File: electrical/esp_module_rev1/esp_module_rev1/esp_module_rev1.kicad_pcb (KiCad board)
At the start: 4 copper layers, 47.2 x 47 mm, 66 parts, among them J1 USB_C_Receptacle_USB2.0_14P, J3 Conn_01x02, Q1 FDN340P, Q2 FDN340P, SW1 SW_Push, SW2 SW_Push, U1 MCP73831-2-OT, U10 BMP390L, U2 USBLC6-2SC6, U3 TLV75533PDBV, U4 TLV75518PDBV, U5 ESP32-C3-WROOM-02, U6 TXS0102DCT, U7 INA180A1, U8 LSM6DS3, U9 MAX30102

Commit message: Layout attempt two. Routing started
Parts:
- added C22: 1uF, Capacitor_SMD:C_0603_1608Metric_Pad1.08x0.95mm_HandSolder, F.Cu at (134.1, 110.8)
- added C23: 1uF, Capacitor_SMD:C_0603_1608Metric_Pad1.08x0.95mm_HandSolder, F.Cu at (161.2, 110.5)
- added TP1: TestPoint, TestPoint:TestPoint_THTPad_D1.5mm_Drill0.7mm, F.Cu at (133.3, 100.0)
- added TP10: TestPoint, TestPoint:TestPoint_THTPad_D1.5mm_Drill0.7mm, F.Cu at (159.3, 83.8)
- added TP11: TestPoint, TestPoint:TestPoint_THTPad_D1.5mm_Drill0.7mm, F.Cu at (159.3, 86.7)
- added TP12: TestPoint, TestPoint:TestPoint_THTPad_D1.5mm_Drill0.7mm, F.Cu at (129.8, 100.0)
- added TP13: TestPoint, TestPoint:TestPoint_THTPad_D1.5mm_Drill0.7mm, F.Cu at (164.6, 99.0)
- added TP14: TestPoint, TestPoint:TestPoint_THTPad_D1.5mm_Drill0.7mm, F.Cu at (136.0, 97.8)
- added TP15: TestPoint, TestPoint:TestPoint_THTPad_D1.5mm_Drill0.7mm, F.Cu at (156.4, 100.3)
- added TP16: TestPoint, TestPoint:TestPoint_THTPad_D1.5mm_Drill0.7mm, F.Cu at (143.4, 105.5)
- added TP17: TestPoint, TestPoint:TestPoint_THTPad_D1.5mm_Drill0.7mm, F.Cu at (148.6, 101.7)
- added TP18: TestPoint, TestPoint:TestPoint_THTPad_D1.5mm_Drill0.7mm, F.Cu at (133.5, 96.0)
- added TP19: TestPoint, TestPoint:TestPoint_THTPad_D1.5mm_Drill0.7mm, F.Cu at (133.2, 87.5)
- added TP2: TestPoint, TestPoint:TestPoint_THTPad_D1.5mm_Drill0.7mm, F.Cu at (131.3, 112.2)
- added TP3: TestPoint, TestPoint:TestPoint_THTPad_D1.5mm_Drill0.7mm, F.Cu at (163.7, 112.2)
- added TP4: TestPoint, TestPoint:TestPoint_THTPad_D1.5mm_Drill0.7mm, F.Cu at (136.2, 108.2)
- added TP5: TestPoint, TestPoint:TestPoint_THTPad_D1.5mm_Drill0.7mm, F.Cu at (156.5, 109.2)
- added TP6: TestPoint, TestPoint:TestPoint_THTPad_D1.5mm_Drill0.7mm, F.Cu at (166.4, 112.3)
- added TP7: TestPoint, TestPoint:TestPoint_THTPad_D1.5mm_Drill0.7mm, F.Cu at (166.2, 109.3)
- added TP8: TestPoint, TestPoint:TestPoint_THTPad_D1.5mm_Drill0.7mm, F.Cu at (128.6, 112.1)
- added TP9: TestPoint, TestPoint:TestPoint_THTPad_D1.5mm_Drill0.7mm, F.Cu at (166.0, 85.8)
- H1, H2, H3: value MountingHole -> MountingHole_Pad; footprint MountingHole:MountingHole_2.2mm_M2 -> MountingHole:MountingHole_2.2mm_M2_Pad_Via
- R4, R5: moved to B.Cu
- moved H2 59.9 mm to (166.3, 119.5)
- moved R22 48.9 mm to (165.2, 102.8), turned to 90 degrees
- moved H1 47.7 mm to (129.3, 119.6)
- moved R16 47.3 mm to (164.8, 92.5), turned to -90 degrees
- moved U10 46.3 mm to (162.9, 102.8)
- moved C20 45.7 mm to (164.7, 107.1)
- moved C21 45.0 mm to (164.7, 105.4)
- moved C11 44.1 mm to (162.3, 87.9), turned to 180 degrees
- moved R15 43.6 mm to (159.8, 93.8), turned to 90 degrees
- moved R17 42.6 mm to (164.8, 89.0), turned to -90 degrees
- moved U6 41.2 mm to (162.3, 91.6), turned to 90 degrees
- moved U3 40.9 mm to (137.0, 113.5), turned to -90 degrees
- moved R6 38.1 mm to (139.6, 114.0), turned to 90 degrees
- moved Q1 37.9 mm to (142.2, 112.8), turned to -90 degrees
- moved C12 37.2 mm to (162.3, 97.0), turned to 0 degrees
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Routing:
- net GND: track 151.6 -> 27.0 mm, vias 8 -> 3
- net +BATT: track 47.7 -> 0.00 mm, vias 6 -> 0
- net /BMP_INT: track 36.2 -> 0.00 mm, vias 2 -> 0
- net Net-(D3-K): track 34.6 -> 0.00 mm, vias 2 -> 0
- net /BOOT_SEL_GPIO9: track 31.5 -> 0.00 mm, vias 1 -> 0
- net /VBATT_SENSE: track 31.2 -> 0.00 mm, vias 2 -> 0
- net /CURR_SENSE: track 30.5 -> 0.00 mm, vias 2 -> 0
- net +3V3: track 39.6 -> 10.9 mm, vias 8 -> 0
- net /USB_CC2: track 31.6 -> 4.24 mm, vias 2 -> 1
- net /LSM_INT2: track 27.2 -> 0.00 mm, vias 2 -> 0
- net Net-(D2-K): track 24.9 -> 0.00 mm, vias 2 -> 0
- net /LSM_INT1: track 18.5 -> 0.00 mm
- net /I2C_SCL: track 15.7 -> 34.1 mm, vias 1 -> 3
- net /I2C_SCL_1V8: track 16.7 -> 1.53 mm
- net +USB_VBUS: track 27.5 -> 14.1 mm
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- removed copper zone on In2.Cu, net +1V8
- removed copper zone on In2.Cu, net +3V3
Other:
- board size 47.2 x 47 mm -> 44.6 x 41.4 mm

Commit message: Routing mostly done i think
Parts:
- moved TP8 32.7 mm to (159.1, 100.3)
- moved R4 2.25 mm to (152.6, 113.0)
- moved R5 2.17 mm to (142.9, 113.0)
- moved U9 1.32 mm to (149.5, 96.0)
- moved TP14 0.25 mm to (136.0, 97.6)
- turned C1 to -90 degrees
- turned R13 to 90 degrees
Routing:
- net GND: track 27.0 -> 124.9 mm, vias 3 -> 13
- net +1V8: track 6.81 -> 100.4 mm, vias 0 -> 2
- net /BOOT_SEL_GPIO9: track 0.00 -> 67.2 mm
- net +BATT: track 0.00 -> 66.5 mm, vias 0 -> 3
- net +3V3: track 10.9 -> 70.3 mm, vias 0 -> 9
- net /ESP32_EN: track 10.3 -> 65.5 mm
- net /I2C_SDA_1V8: track 0.00 -> 53.5 mm, vias 0 -> 2
- net /BMP_INT: track 0.00 -> 46.6 mm, vias 0 -> 1
- net /VBATT_SENSE: track 0.00 -> 42.7 mm, vias 0 -> 2
- net /CURR_SENSE: track 0.00 -> 41.5 mm, vias 0 -> 2
- net /I2C_SCL_1V8: track 1.53 -> 37.8 mm, vias 0 -> 2
- net /I2C_SDA: track 5.75 -> 41.8 mm, vias 0 -> 2
- net /MAX_INT: track 0.00 -> 34.7 mm, vias 0 -> 2
- net /LSM_INT2: track 0.00 -> 33.9 mm, vias 0 -> 2
- net /USB_D+: track 0.00 -> 29.1 mm, vias 0 -> 2
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- added copper zone on In2.Cu, net +3V3

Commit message: Responding to comments
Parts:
- removed R17: 5k1, Resistor_SMD:R_0603_1608Metric_Pad0.98x0.95mm_HandSolder
- added C24: 0u1, Capacitor_SMD:C_0603_1608Metric_Pad1.08x0.95mm_HandSolder, F.Cu at (139.7, 101.6)
- added R23: 5k1, Resistor_SMD:R_0603_1608Metric_Pad0.98x0.95mm_HandSolder, B.Cu at (152.7, 84.6)
- C1, C2: value 10uF -> 4u7
- C14: value 10uF -> 100n
- C15: value 0u1F -> 100n
- C16: value 0u1F -> 4u7
- C17, C18: value 0u1F -> 0u1
- C19: value 1uF -> 10u
- C5, C6: value 10uF -> 1uF
- R13, R15, R2: value 5k1 -> 1k5
- R14: moved to B.Cu
- R16: value 5k1 -> 10k
- U7: value INA180A1 -> INA180A2
- moved R14 20.2 mm to (140.2, 85.5), turned to -90 degrees
- moved TP11 9.36 mm to (168.4, 84.5)
- moved R16 8.42 mm to (159.4, 86.0), turned to 180 degrees
- moved TP4 8.21 mm to (128.7, 111.6)
- moved R5 7.43 mm to (146.5, 119.5), turned to -90 degrees
- moved R4 7.18 mm to (149.5, 119.5), turned to -90 degrees
- moved R19 6.73 mm to (136.3, 108.3), turned to 180 degrees
- moved R18 4.42 mm to (136.3, 106.7), turned to 0 degrees
- moved R15 3.92 mm to (158.4, 90.1)
- moved R20 3.53 mm to (138.0, 104.7)
- moved U7 2.45 mm to (136.7, 101.4), turned to 0 degrees
- moved TP12 1.84 mm to (128.0, 99.6)
- moved C11 1.30 mm to (163.4, 87.2), turned to 90 degrees
- moved TP1 0.30 mm to (133.0, 100.0)
- renumbered SW2 to BOOT, SW1 to RST
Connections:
- R14 pad 2: /I2C_SDA -> /MAX_INT
- R15 pad 2: /I2C_SCL -> /USB_D+
- R16 pad 1: +1V8 -> Net-(R16-Pad1)
- R16 pad 2: /I2C_SCL_1V8 -> /CURR_SENSE
- TP11 pad 1: /CURR_SENSE -> Net-(R16-Pad1)
- U5 pad 16: unconnected-(U5-IO2-Pad16) -> Net-(U5-IO2)
- U7 pad 1: /CURR_SENSE -> Net-(R16-Pad1)
- U7 pad 3: +BATT -> Net-(J3-Pin_1)
- U7 pad 4: Net-(J3-Pin_1) -> +BATT
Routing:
- net Net-(R16-Pad1): track 0.00 -> 53.1 mm, vias 0 -> 3
- net /CURR_SENSE: track 41.5 -> 2.86 mm, vias 2 -> 0
- net +3V3: track 70.3 -> 88.7 mm, vias 9 -> 10
- net /VBATT_SENSE: track 42.7 -> 55.6 mm
- net Net-(D2-K): track 11.8 -> 20.6 mm, vias 0 -> 1
- net +BATT: track 66.5 -> 75.0 mm, vias 3 -> 4
- net /USB_CC1: track 7.19 -> 2.62 mm
- net +1V8: track 100.4 -> 96.0 mm
- net /USB_CC2: track 6.74 -> 2.62 mm
- net Net-(U5-IO2): track 0.00 -> 4.04 mm, vias 0 -> 1
- net /MAX_INT: track 34.7 -> 37.4 mm
- net /USB_D+: track 29.1 -> 31.7 mm
- net /USB_D-: track 28.6 -> 30.6 mm
- net GND: track 124.9 -> 126.6 mm
- net /I2C_SDA: track 41.8 -> 42.9 mm
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
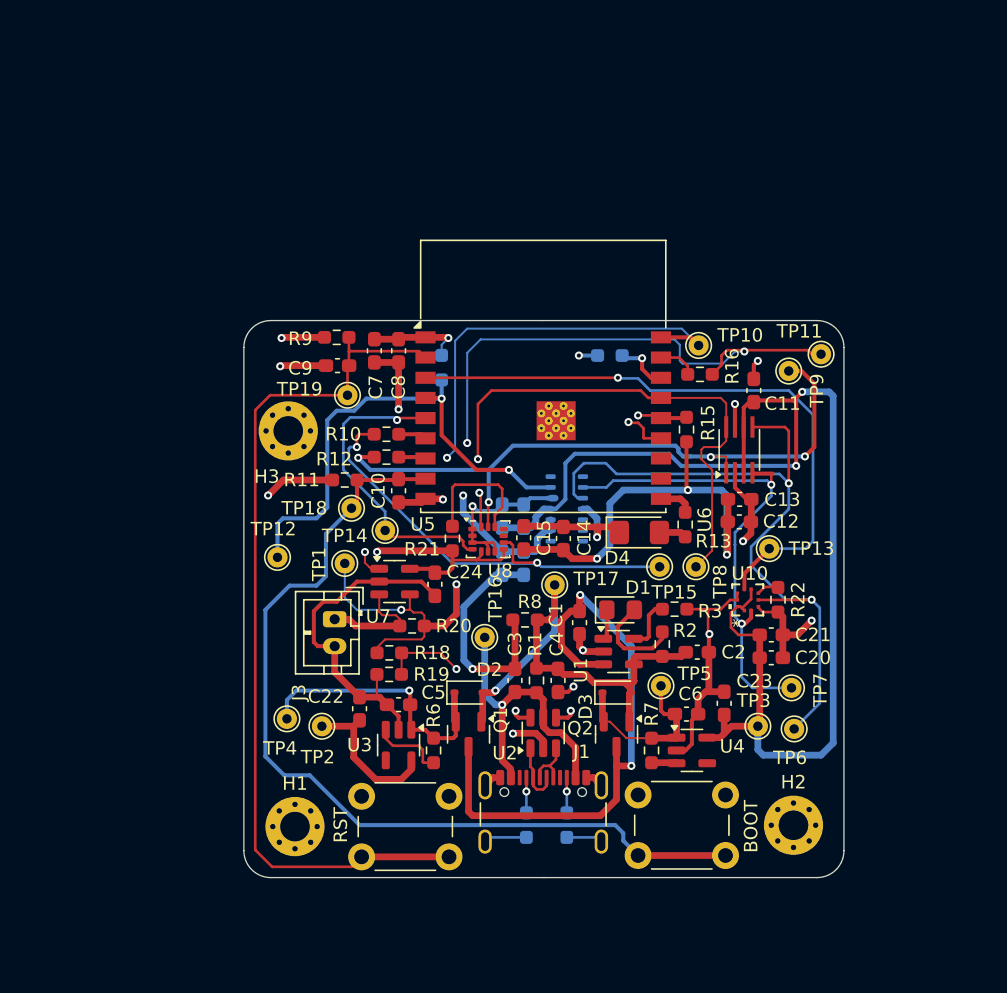
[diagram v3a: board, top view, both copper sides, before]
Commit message: Revised USB layout and ground pour on bottom layer
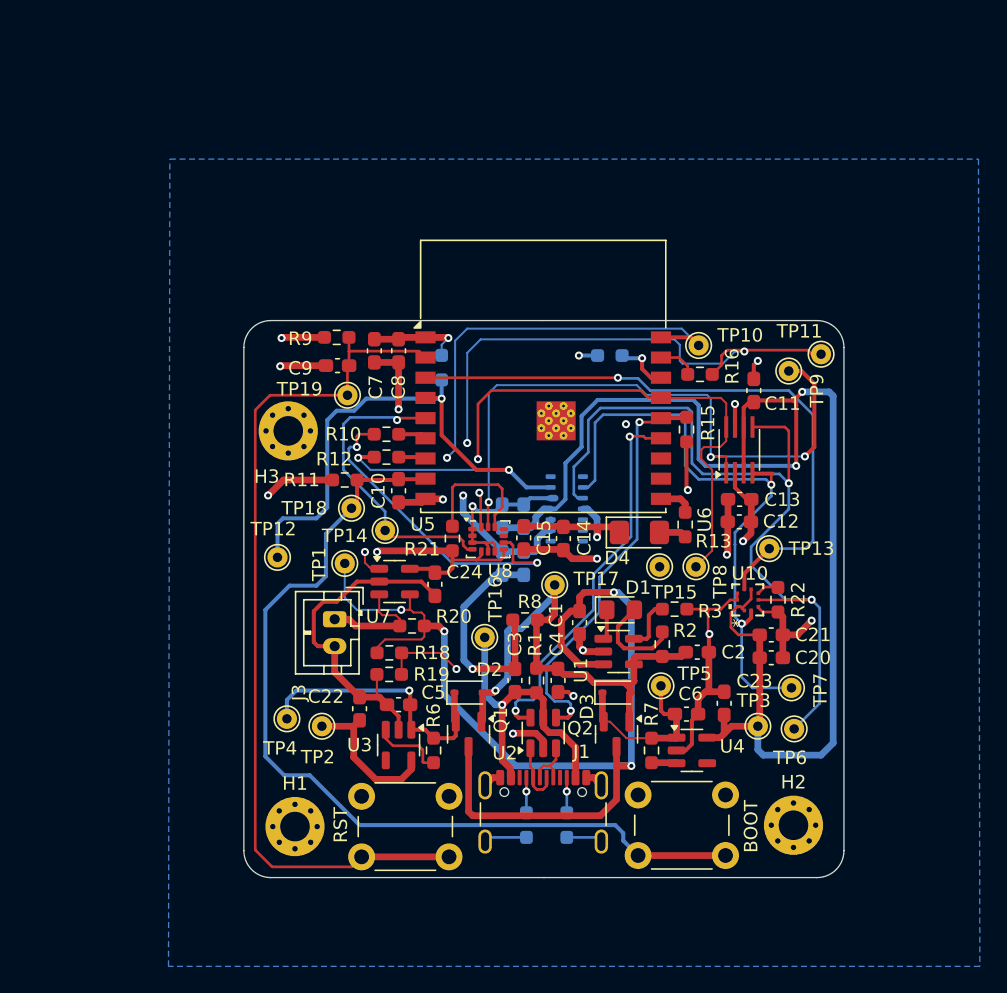
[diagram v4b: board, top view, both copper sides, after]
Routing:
- net +3V3: track 88.7 -> 70.5 mm
- net /I2C_SCL: track 50.6 -> 60.1 mm
- net +BATT: track 75.0 -> 84.4 mm
- net /I2C_SCL_1V8: track 37.8 -> 46.4 mm
- net /I2C_SDA_1V8: track 53.4 -> 60.7 mm
- net +1V8: track 96.0 -> 103.0 mm
- net /USB_D-: track 30.6 -> 28.5 mm
- net /USB_D+: track 31.7 -> 30.8 mm
- net GND: vias 13 -> 14
- added copper zone on B.Cu, net GND

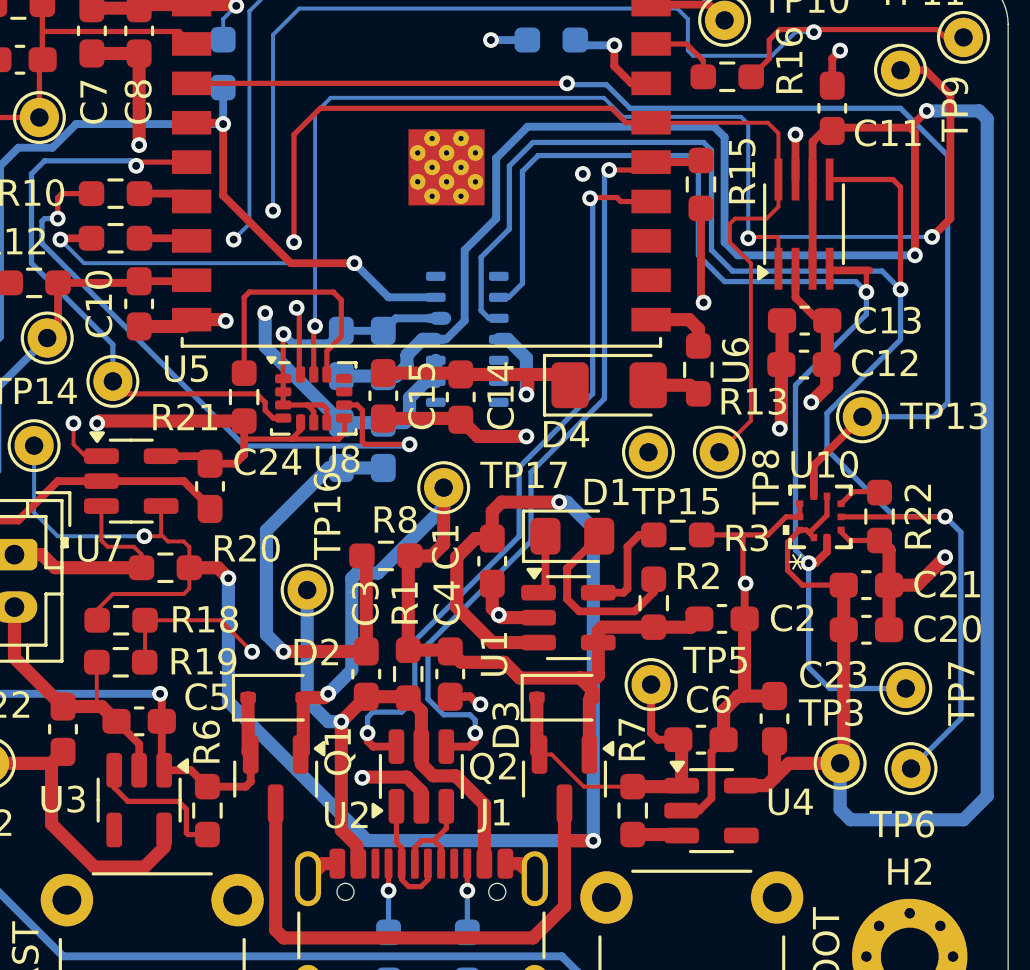
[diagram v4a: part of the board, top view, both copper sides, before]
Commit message: Trace is no longer broken
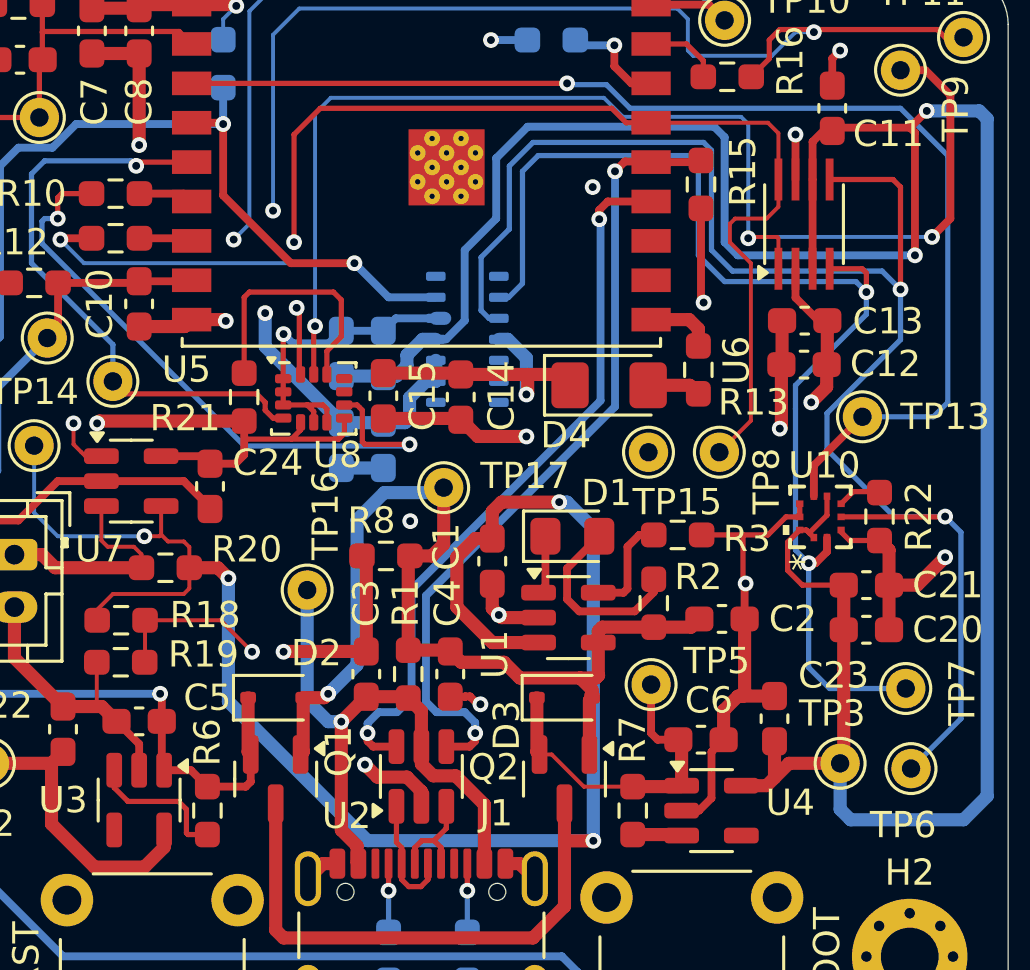
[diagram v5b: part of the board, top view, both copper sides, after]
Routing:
- net GND: track 126.6 -> 117.9 mm, vias 14 -> 15
- net /USB_D-: track 28.5 -> 27.7 mm
- net +USB_VBUSF: track 37.2 -> 37.9 mm

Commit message: Pushing unsaved changes
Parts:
- J3: footprint Connector_JST:JST_PH_B2B-PH-K_1x02_P2.00mm_Vertical -> Connector_JST:JST_GH_BM02B-GHS-TBT_1x02-1MP_P1.25mm_Vertical
- moved J3 1.93 mm to (130.6, 105.2), turned to 90 degrees
- renumbered RST to SW1, BOOT to SW2
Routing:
- net GND: track 117.9 -> 113.7 mm, vias 15 -> 17
- net Net-(J3-Pin_1): track 8.61 -> 9.47 mm
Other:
- board text added: "+BATT"
- board text added: "Adel C"
